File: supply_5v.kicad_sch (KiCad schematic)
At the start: 13 parts, among them IC2 TPS564242DRLR

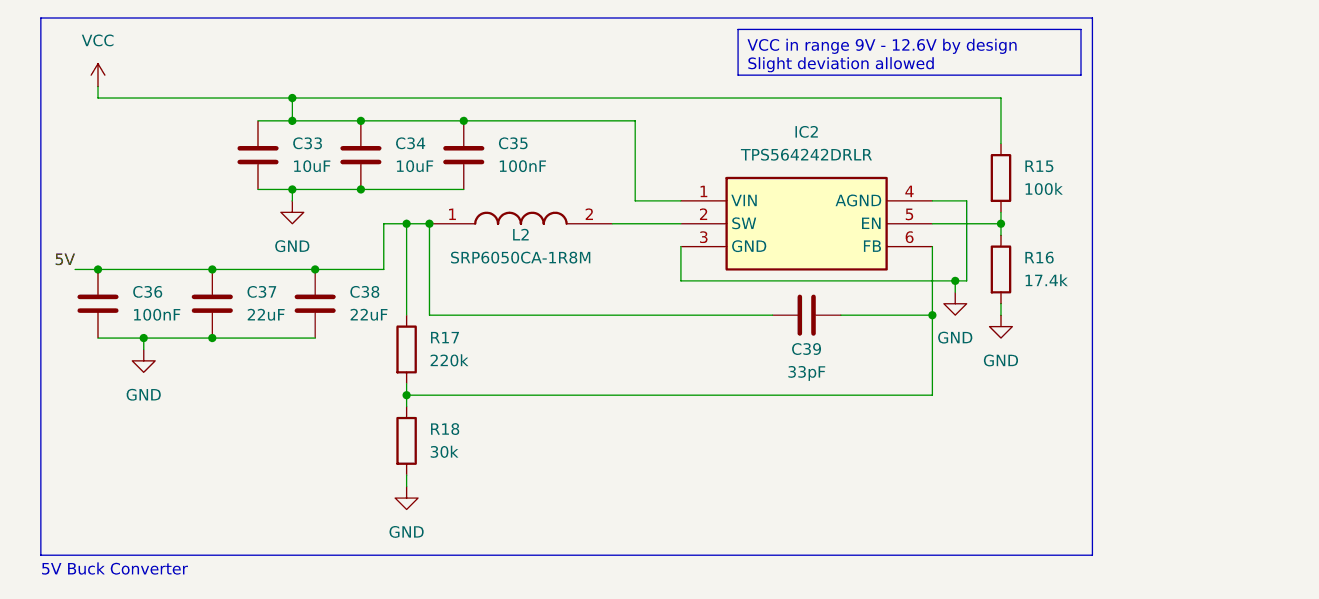
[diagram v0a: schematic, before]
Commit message: Added required connectors for this version
Also did some file name changes
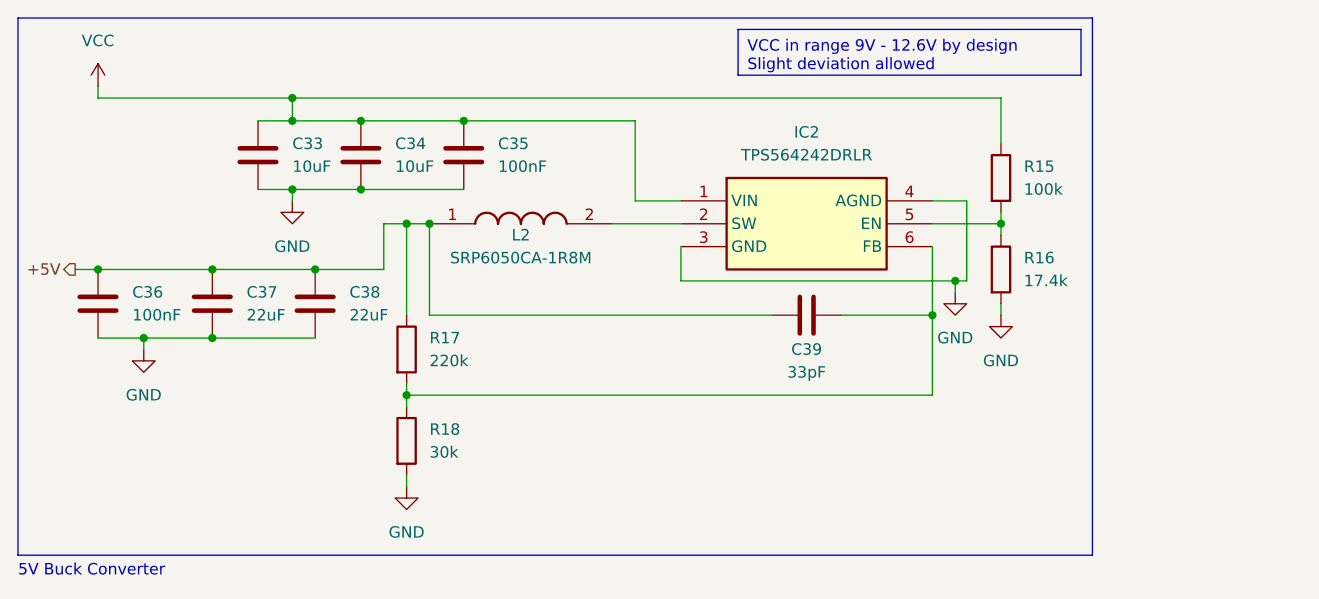
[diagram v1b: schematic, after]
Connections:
- net 5V renamed +5V
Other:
- title: Buck Converter with 5V output -> 5V Supply
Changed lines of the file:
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@@
   (paper "A4")
   (title_block
-    (title "Buck Converter with 5V output")
-    (date "2023-11-01")
+    (title "5V Supply")
+    (date "2023-11-23")
     (rev "0.1")
   )
@@
     (stroke (width 0) (type default))
   )
-  (rectangle (start 25.4 25.4) (end 142.24 85.09)
+  (rectangle (start 22.86 25.4) (end 142.24 85.09)
     (stroke (width 0) (type default))
     (fill (type none))
@@
     (effects (font (size 1.27 1.27)) (justify left top))
   )
-  (text "5V Buck Converter" (at 25.4 87.63 0)
+  (text "5V Buck Converter" (at 22.86 87.63 0)
     (effects (font (size 1.27 1.27)) (justify left bottom))
   )
-  (label "5V" (at 29.21 53.34 180) (fields_autoplaced)
-    (effects (font (size 1.27 1.27)) (justify right bottom))
+  (hierarchical_label "+5V" (shape output) (at 29.21 53.34 180) (fields_autoplaced)
+    (effects (font (size 1.27 1.27)) (justify right))
   )
   (symbol (lib_id "Device:C") (at 55.88 57.15 0) (unit 1)
@@
     (pin "2")
     (instances
-      (project "PSU_module_minirys"
+      (project "rpiboard_minirys"
         (path "/83ec67aa-411e-440d-8530-858fb57a6552"
           (reference "C38") (unit 1)
@@
     (pin "2")
     (instances
-      (project "PSU_module_minirys"
+      (project "rpiboard_minirys"
         (path "/83ec67aa-411e-440d-8530-858fb57a6552"
           (reference "R17") (unit 1)
@@
     (pin "1")
     (instances
-      (project "PSU_module_minirys"
+      (project "rpiboard_minirys"
         (path "/83ec67aa-411e-440d-8530-858fb57a6552"
           (reference "#PWR028") (unit 1)
@@
     (pin "2")
     (instances
-      (project "PSU_module_minirys"
+      (project "rpiboard_minirys"
         (path "/83ec67aa-411e-440d-8530-858fb57a6552"
           (reference "C36") (unit 1)
@@
     (pin "2")
     (instances
-      (project "PSU_module_minirys"
+      (project "rpiboard_minirys"
         (path "/83ec67aa-411e-440d-8530-858fb57a6552"
           (reference "R15") (unit 1)
@@
     (pin "1")
     (instances
-      (project "PSU_module_minirys"
+      (project "rpiboard_minirys"
         (path "/83ec67aa-411e-440d-8530-858fb57a6552"
           (reference "#PWR029") (unit 1)
@@
     (pin "2")
     (instances
-      (project "PSU_module_minirys"
+      (project "rpiboard_minirys"
         (path "/83ec67aa-411e-440d-8530-858fb57a6552"
           (reference "R16") (unit 1)
@@
     (pin "1")
     (instances
-      (project "PSU_module_minirys"
+      (project "rpiboard_minirys"
         (path "/83ec67aa-411e-440d-8530-858fb57a6552"
           (reference "#PWR027") (unit 1)
@@
     (pin "2")
     (instances
-      (project "PSU_module_minirys"
+      (project "rpiboard_minirys"
         (path "/83ec67aa-411e-440d-8530-858fb57a6552"
           (reference "C39") (unit 1)
@@
     (pin "2")
     (instances
-      (project "PSU_module_minirys"
+      (project "rpiboard_minirys"
         (path "/83ec67aa-411e-440d-8530-858fb57a6552"
           (reference "C34") (unit 1)
@@
     (pin "2")
     (instances
-      (project "PSU_module_minirys"
+      (project "rpiboard_minirys"
         (path "/83ec67aa-411e-440d-8530-858fb57a6552"
           (reference "R18") (unit 1)
@@
     (pin "2")
     (instances
-      (project "PSU_module_minirys"
+      (project "rpiboard_minirys"
         (path "/83ec67aa-411e-440d-8530-858fb57a6552"
           (reference "L2") (unit 1)
@@
     (pin "1")
     (instances
-      (project "PSU_module_minirys"
+      (project "rpiboard_minirys"
         (path "/83ec67aa-411e-440d-8530-858fb57a6552"
           (reference "#PWR023") (unit 1)
@@
     (pin "2")
     (instances
-      (project "PSU_module_minirys"
+      (project "rpiboard_minirys"
         (path "/83ec67aa-411e-440d-8530-858fb57a6552"
           (reference "C35") (unit 1)
@@
     (pin "2")
     (instances
-      (project "PSU_module_minirys"
+      (project "rpiboard_minirys"
         (path "/83ec67aa-411e-440d-8530-858fb57a6552"
           (reference "C37") (unit 1)
@@
     (pin "2")
     (instances
-      (project "PSU_module_minirys"
+      (project "rpiboard_minirys"
         (path "/83ec67aa-411e-440d-8530-858fb57a6552"
           (reference "C33") (unit 1)
@@
     (pin "6")
     (instances
-      (project "PSU_module_minirys"
+      (project "rpiboard_minirys"
         (path "/83ec67aa-411e-440d-8530-858fb57a6552"
           (reference "IC2") (unit 1)
@@
     (pin "1")
     (instances
-      (project "PSU_module_minirys"
+      (project "rpiboard_minirys"
         (path "/83ec67aa-411e-440d-8530-858fb57a6552"
           (reference "#PWR030") (unit 1)
@@
     (pin "1")
     (instances
-      (project "PSU_module_minirys"
+      (project "rpiboard_minirys"
         (path "/83ec67aa-411e-440d-8530-858fb57a6552"
           (reference "#PWR031") (unit 1)

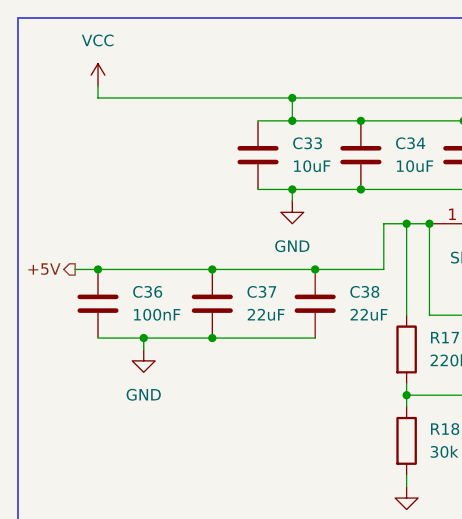
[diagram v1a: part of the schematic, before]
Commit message: Finished motor drivers schematic
Still need to connect all the connectors and sort out old unused connections
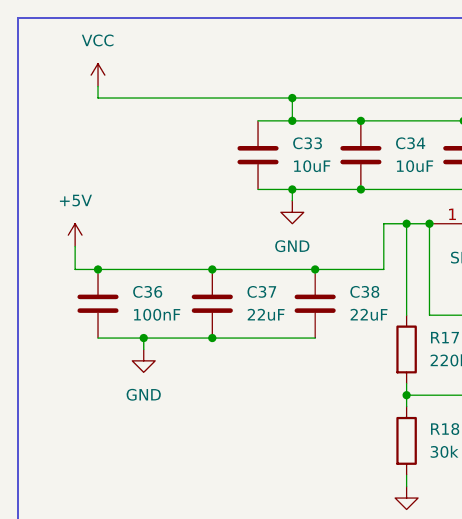
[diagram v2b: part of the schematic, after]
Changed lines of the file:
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@@
   (title_block
     (title "5V Supply")
-    (date "2023-11-23")
-    (rev "0.1")
+    (date "2023-11-29")
+    (rev "1.0")
   )
   (junction (at 53.34 44.45) (diameter 0) (color 0 0 0 0)
@@
   )
   (wire (pts (xy 132.08 48.26) (xy 132.08 49.53))
+    (stroke (width 0) (type default))
+  )
+  (wire (pts (xy 29.21 50.8) (xy 29.21 53.34))
     (stroke (width 0) (type default))
   )
@@
   (text "5V Buck Converter" (at 22.86 87.63 0)
     (effects (font (size 1.27 1.27)) (justify left bottom))
-  )
-  (hierarchical_label "+5V" (shape output) (at 29.21 53.34 180) (fields_autoplaced)
-    (effects (font (size 1.27 1.27)) (justify right))
   )
   (symbol (lib_id "Device:C") (at 55.88 57.15 0) (unit 1)
@@
         )
       )
+    )
+  )
+  (symbol (lib_id "power:+5V") (at 29.21 50.8 0) (unit 1)
+    (in_bom yes) (on_board yes) (dnp no) (fields_autoplaced)
+    (property "Reference" "#PWR032" (at 29.21 54.61 0)
+      (effects (font (size 1.27 1.27)) hide)
+    )
+    (property "Value" "+5V" (at 29.21 45.72 0)
+      (effects (font (size 1.27 1.27)))
+    )
+    (property "Footprint" "" (at 29.21 50.8 0)
+      (effects (font (size 1.27 1.27)) hide)
+    )
+    (property "Datasheet" "" (at 29.21 50.8 0)
+      (effects (font (size 1.27 1.27)) hide)
+    )
+    (pin "1")
+    (instances
+      (project "rpiboard_minirys"
+        (path "/83ec67aa-411e-440d-8530-858fb57a6552/eeb2755d-fcb9-485d-956d-83c372a71240"
+          (reference "#PWR032") (unit 1)
+        )
+      )

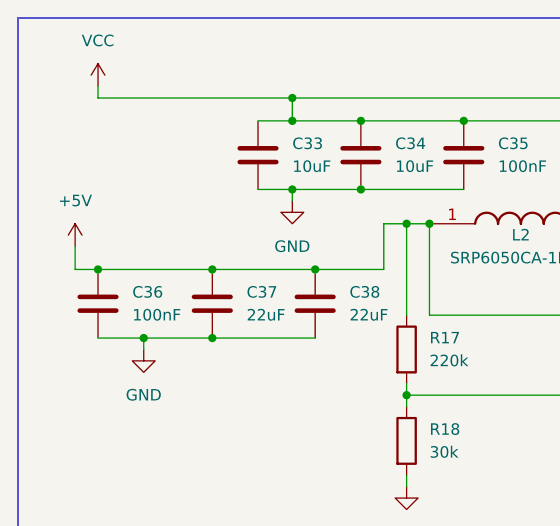
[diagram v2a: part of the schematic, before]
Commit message: New complete schematic version
May need to resize the resistors, also need to change the caps back to electrolytic
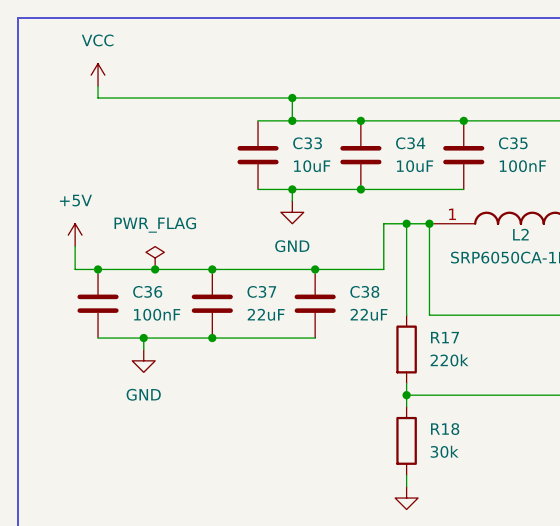
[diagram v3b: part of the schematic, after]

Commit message: Uploaded all project files, finished PCB design
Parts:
- removed C37, C38: 22uF, Capacitor_SMD:C_0805_2012Metric, symbol Device:C
- added C33 (x4): 10uF, Capacitor_SMD:C_0805_2012Metric, symbol Device:C
- L2: symbol parts:SRP6050CA-1R8M -> Device:L
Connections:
- net +5V: now also C33.1, C33.1, C33.1, C33.1
- net GND: now also C33.2, C33.2, C33.2, C33.2
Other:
- note added: "1.8uH"
- moved on the sheet: C33, C34, C35, C36, C39, IC2, R15, R16, R17, R18
